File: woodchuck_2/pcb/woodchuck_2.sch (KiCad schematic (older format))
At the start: 31 parts

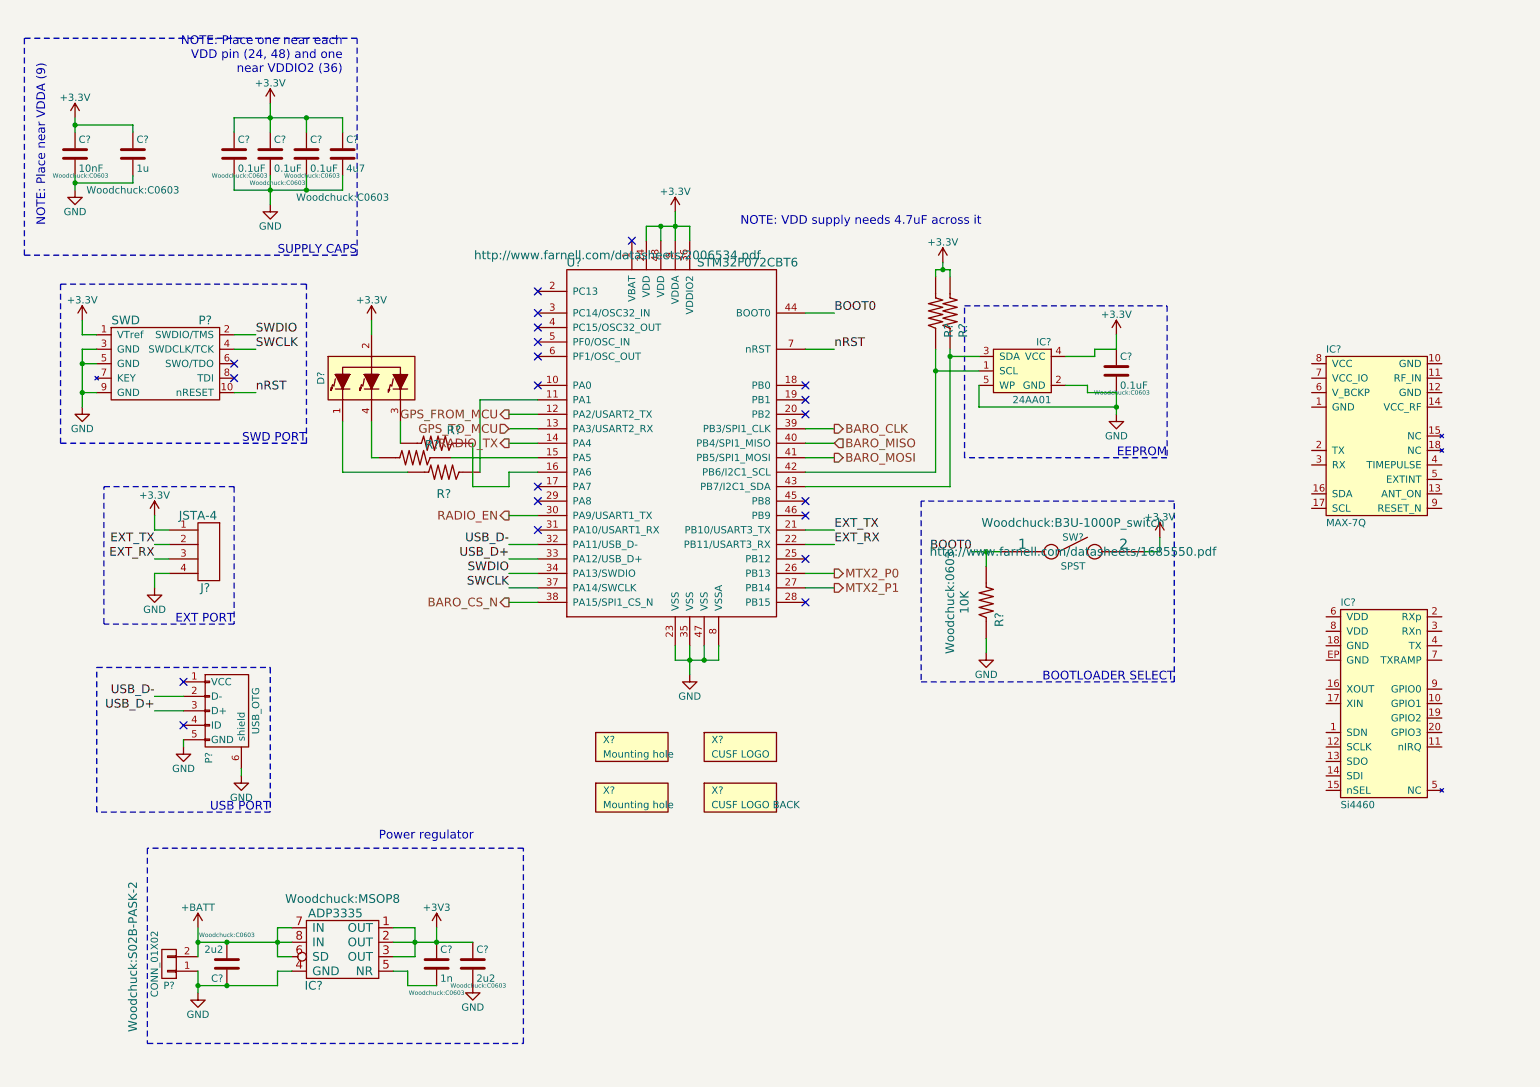
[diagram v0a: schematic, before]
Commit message: Tidy up files in branch, add radio and GPS to schematic, remove barometer, USART, USB
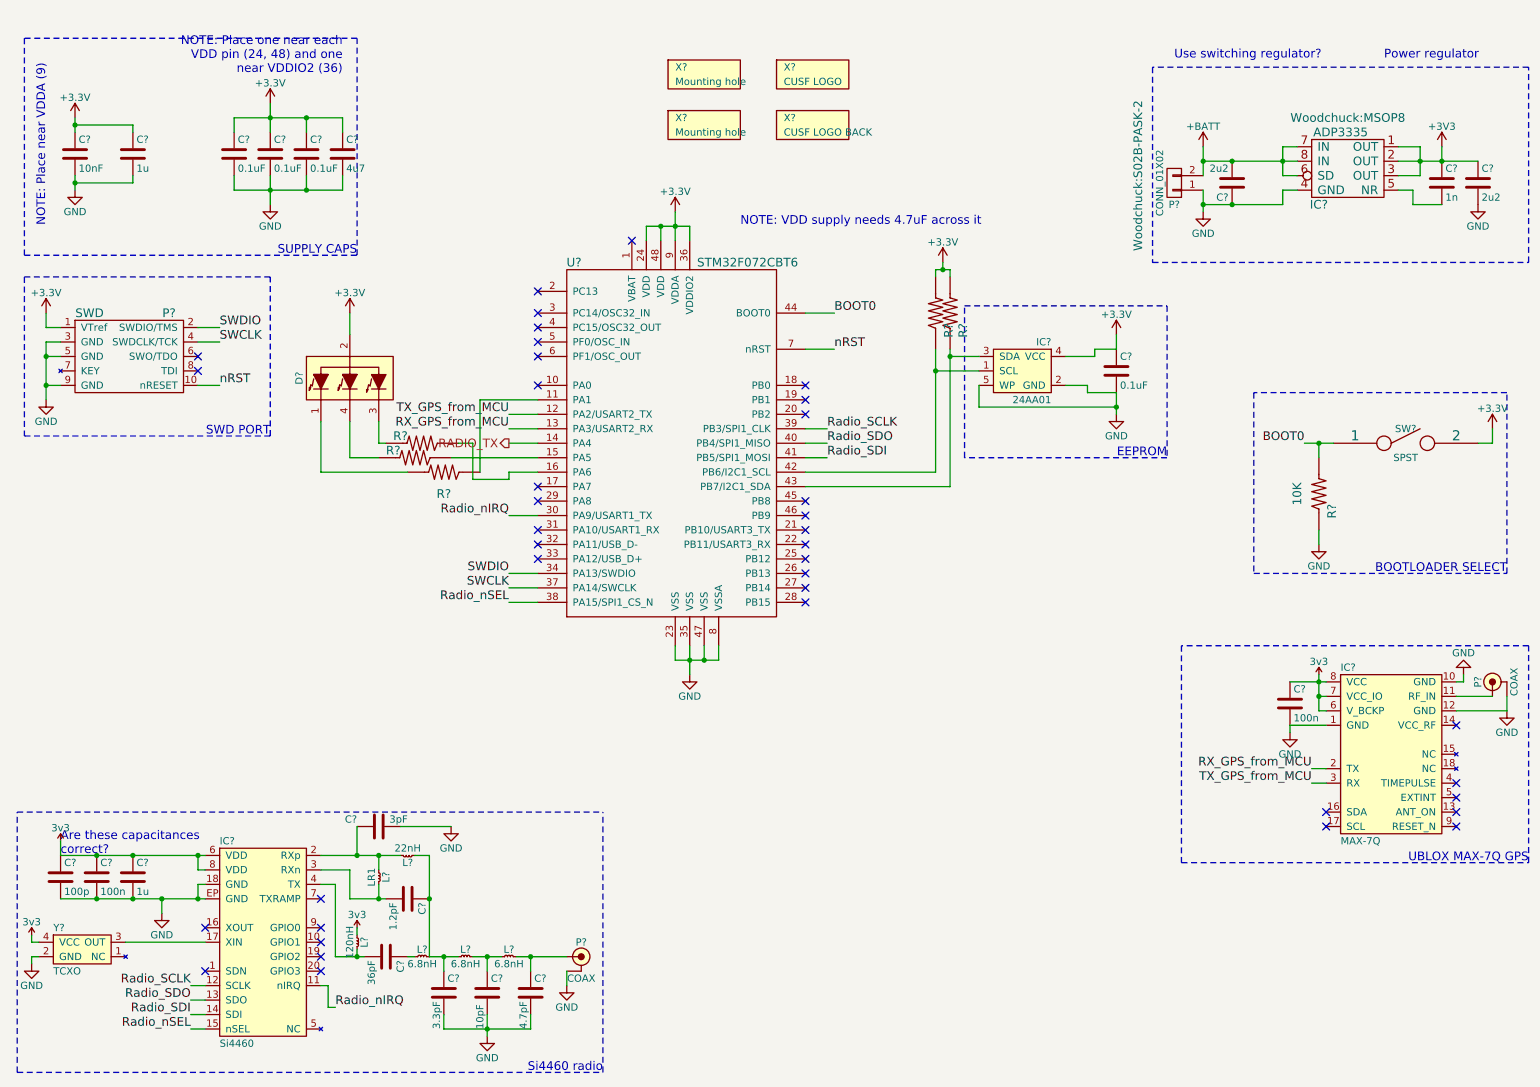
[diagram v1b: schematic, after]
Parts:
- removed J?: JSTA-4, Woodchuck:S04B-PASK-2, symbol JSTA-4
- removed P?: USB_OTG, Woodchuck:MOLEX_67503_1020_MINI_USB, symbol USB_OTG
- added C? (x2): 100n, agg:0402, symbol C
- added C?: 1u, agg:0402, symbol C
- added C?: 100p, agg:0402, symbol C
- added C?: 3pF, agg:0402, symbol C
- added C?: 1.2pF, agg:0402, symbol C
- added C?: 36pF, agg:0402, symbol C
- added C?: 3.3pF, agg:0402, symbol C
- added C?: 10pF, agg:0402, symbol C
- added C?: 4.7pF, agg:0402, symbol C
- added L?: LR1, agg:0603-L, symbol L
- added L?: 22nH, agg:0603-L, symbol L
- added L?: 120nH, agg:0603-L, symbol L
- added L? (x3): 6.8nH, agg:0603-L, symbol L
- added P? (x2): COAX, agg-unchecked:SMA-142-0701-801, symbol COAX
- added Y?: TCXO, symbol TCXO
- C? (x2): Digikey (none) -> Value; Farnell (none) -> Value; Fieldname (none) -> Value
- SW?: Digikey (none) -> Value; Fieldname (none) -> Value
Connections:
- net BARO_CLK is gone; now on net Radio_SCLK: U?.39 (PB3/SPI1_CLK)
- net BARO_CS_N is gone; now on net Radio_nSEL: U?.38 (PA15/SPI1_CS_N)
- net BARO_MISO is gone; now on net Radio_SDO: U?.40 (PB4/SPI1_MISO)
- net BARO_MOSI is gone; now on net Radio_SDI: U?.41 (PB5/SPI1_MOSI)
- net GPS_FROM_MCU is gone; now on net TX_GPS_from_MCU: U?.12 (PA2/USART2_TX)
- net GPS_TO_MCU is gone; now on net RX_GPS_from_MCU: U?.13 (PA3/USART2_RX)
- net RADIO_EN is gone; now on net Radio_nIRQ: U?.30 (PA9/USART1_TX)
- net GND: now also IC?.1 (GND), IC?.10 (GND), IC?.12 (GND), IC?.18 (GND), IC?.EP (GND), C?.2, C?.2, C?.2, C?.2, C?.2, C?.2, C?.2, C?.2, P?.2 (GND), P?.2 (GND), Y?.2 (GND)
- net at IC?.11 (RF_IN): now also P?.1 (RF)
- net RX_GPS_from_MCU: now reaches IC?.2 (TX)
- net TX_GPS_from_MCU: now reaches IC?.3 (RX)
- net 3v3: now reaches IC?.6 (V_BCKP)
- net 3v3: now also IC?.6 (VDD), IC?.7 (VCC_IO), IC?.8 (VCC), IC?.8 (VDD), C?.1, C?.1, C?.1, C?.1, L?.1, Y?.4 (VCC)
- net Radio_nIRQ: now reaches IC?.11 (nIRQ)
- net Radio_SCLK: now reaches IC?.12 (SCLK)
- net Radio_SDO: now reaches IC?.13 (SDO)
- net Radio_SDI: now reaches IC?.14 (SDI)
- net Radio_nSEL: now reaches IC?.15 (nSEL)
- net at IC?.17 (XIN): now also Y?.3 (OUT)
- net at IC?.2 (RXp): now also C?.1, L?.1, L?.2
- net at IC?.3 (RXn): now also C?.2, L?.2
- net at IC?.4 (TX): now also C?.2, L?.2
- net EXT_RX: no longer names the net of U?.22 (PB11/USART3_RX)
- net EXT_TX: no longer names the net of U?.21 (PB10/USART3_TX)
- net MTX2_P0: no longer names the net of U?.26 (PB13)
- net MTX2_P1: no longer names the net of U?.27 (PB14)
- net USB_D+: no longer names the net of U?.33 (PA12/USB_D+)
- net USB_D-: no longer names the net of U?.32 (PA11/USB_D-)
- new net: C?.1, C?.1, L?.1, L?.1, L?.2
- new net: C?.1, L?.1
- new net: C?.1, L?.1, L?.2
- new net: C?.1, L?.2, P?.1 (RF)
- no-connect marks 21 -> 39
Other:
- note added: "Are these capacitances\ncorrect?\n"
- note added: "Si4460 radio"
- note added: "UBLOX MAX-7Q GPS"
- note added: "Use switching regulator?"
- note removed: "EXT PORT"
- note removed: "USB PORT"
- moved on the sheet: C?, D?, IC?, P?, R?, SW?, X?

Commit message: Tidy up folders
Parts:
- removed D?: LED_RABG, Woodchuck:CREE_RGB_LED, symbol LED_RABG
- removed R?: 10K, Woodchuck:0603, symbol RESISTOR
- removed R? (x2): 510, Woodchuck:0603, symbol RESISTOR
- removed SW?: SPST, Woodchuck:B3U-1000P_switch, symbol SPST
- added D1: LED, symbol LED
- added R4: 10K, Woodchuck:0603, symbol RESISTOR
- added TP1: TESTPAD, agg:TESTPAD, symbol TESTPAD
- C4: renamed from C?; footprint Woodchuck:C0603 -> agg:0402; Farnell Value -> 2496814
- gave numbers to parts that had none: 42
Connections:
- net 3v3 is gone; now on net +3V3: C1.1, C18.1, C3.1, C5.1, IC1.6 (VDD), IC1.8 (VDD), IC4.6 (V_BCKP), IC4.7 (VCC_IO), IC4.8 (VCC), L1.1, Y1.4 (VCC)
- net +3V3: now also D1.2 (A)
- net GND: now also R4.1
- net Radio_nIRQ: now also U1.33 (PA12/USB_D+); no longer U1.30 (PA9/USART1_TX)
- net at R1.1: now also D1.1 (K)
- net BOOT0: no longer names the net of U1.44 (BOOT0)
- net BOOT0: now also R4.2, TP1.1 (TP)
- net RADIO_TX: no longer names the net of U1.14 (PA4)
- no-connect marks 39 -> 42
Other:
- note removed: "BOOTLOADER SELECT"
- note removed: "Use switching regulator?"
- moved on the sheet: R1

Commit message: Use KIPRJMOD in footprint library paths
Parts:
- IC4: footprint agg-unchecked:MAX-7Q -> unchecked:MAX-7Q; Digikey (none) -> Value; Farnell (none) -> Value; Fieldname (none) -> Value
- P2, P4: footprint agg-unchecked:SMA-142-0701-801 -> unchecked:SMA-142-0701-801; Digikey (none) -> Value; Fieldname (none) -> Value
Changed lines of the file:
@@
 F 0 "IC4" H 9700 5950 50  0000 L CNN
 F 1 "MAX-7Q" H 9700 4750 50  0000 L CNN
-F 2 "agg-unchecked:MAX-7Q" H 9700 4650 50  0001 L CNN
+F 2 "unchecked:MAX-7Q" H 9700 4650 50  0001 L CNN
 F 3 "" H 10050 5450 50  0001 C CNN
-F 4 "MAX-7Q" H 9700 4550 50  0001 L CNN "HabSupplies"
+F 4 "Value" H 10100 5450 60  0001 C CNN "Digikey"
+F 5 "Value" H 10100 5450 60  0001 C CNN "Farnell"
+F 6 "Value" H 10100 5450 60  0001 C CNN "Fieldname"
+F 7 "MAX-7Q" H 9700 4550 50  0001 L CNN "HabSupplies"
 	1    10100 5450
 	1    0    0    -1
@@
 F 0 "P4" H 10750 5150 50  0000 C CNN
 F 1 "COAX" H 10750 4900 50  0000 C CNN
-F 2 "agg-unchecked:SMA-142-0701-801" H 10750 4840 50  0001 C CNN
+F 2 "unchecked:SMA-142-0701-801" H 10750 4840 50  0001 C CNN
 F 3 "" H 10850 4950 50  0001 C CNN
-F 4 "1608592" H 10750 4770 50  0001 C CNN "Farnell"
+F 4 "Value" H 10750 5050 60  0001 C CNN "Digikey"
+F 5 "1608592" H 10750 4770 50  0001 C CNN "Farnell"
+F 6 "Value" H 10750 5050 60  0001 C CNN "Fieldname"
 	1    10750 5050
 	0    -1   -1   0
@@
 F 0 "P2" H 4450 7050 50  0000 C CNN
 F 1 "COAX" H 4450 6800 50  0000 C CNN
-F 2 "agg-unchecked:SMA-142-0701-801" H 4450 6740 50  0001 C CNN
+F 2 "unchecked:SMA-142-0701-801" H 4450 6740 50  0001 C CNN
 F 3 "" H 4550 6850 50  0001 C CNN
-F 4 "1608592" H 4450 6670 50  0001 C CNN "Farnell"
+F 4 "Value" H 4450 6950 60  0001 C CNN "Digikey"
+F 5 "1608592" H 4450 6670 50  0001 C CNN "Farnell"
+F 6 "Value" H 4450 6950 60  0001 C CNN "Fieldname"
 	1    4450 6950
 	1    0    0    -1

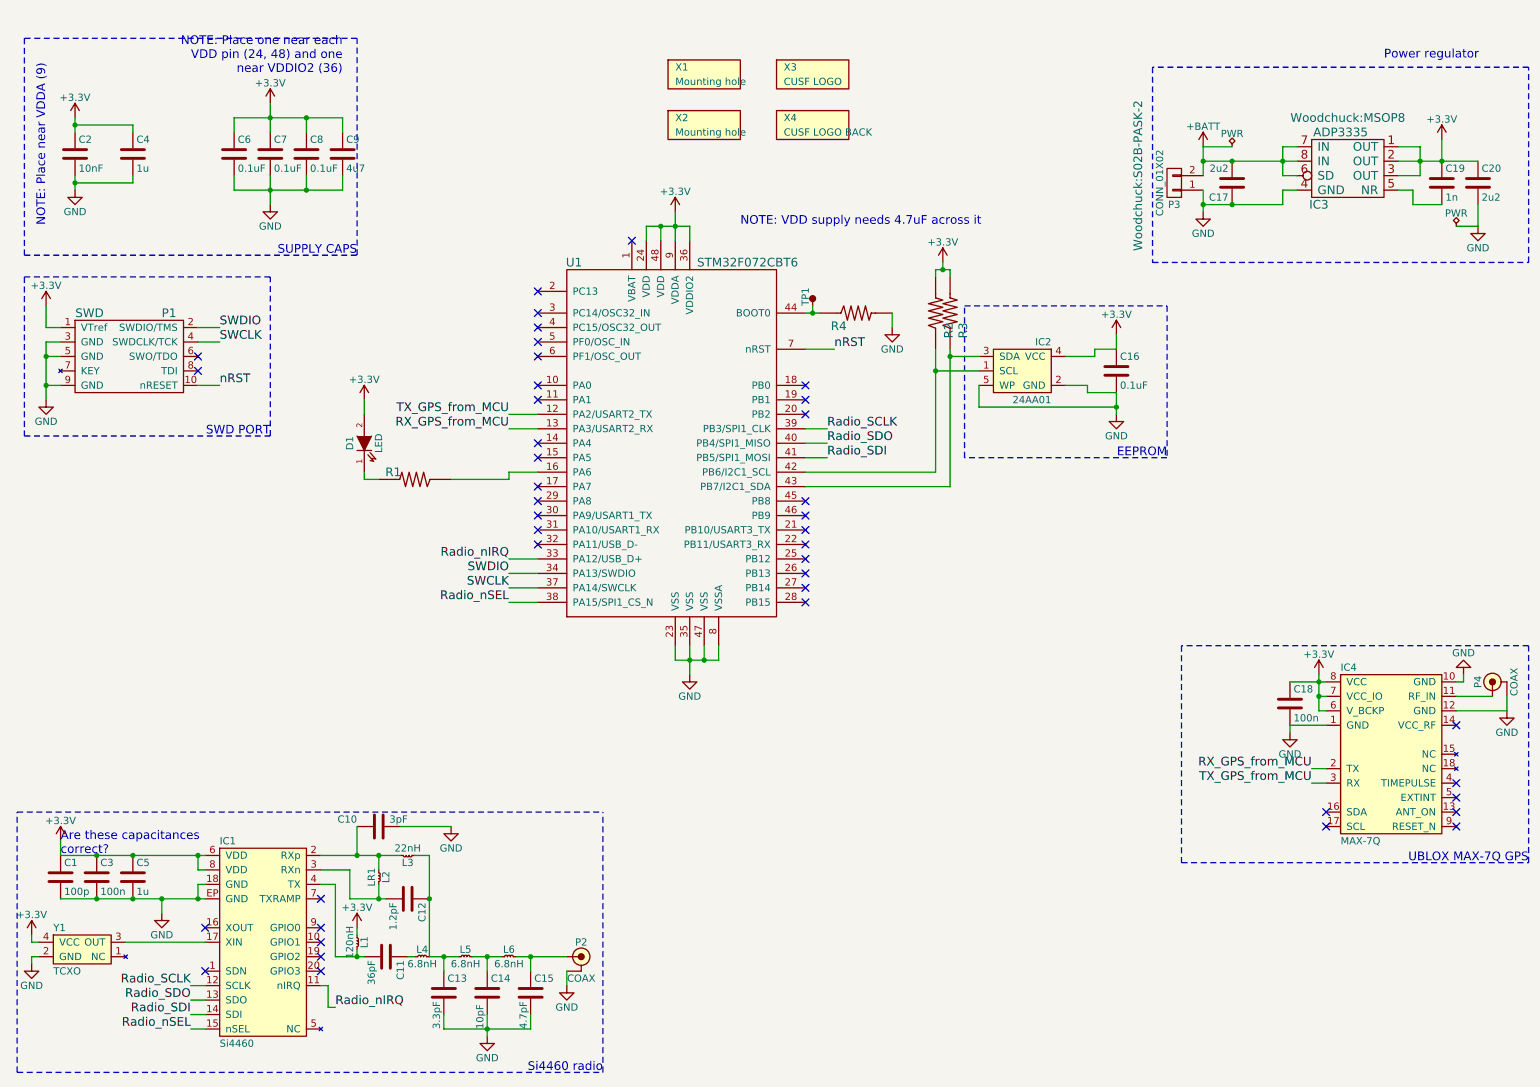
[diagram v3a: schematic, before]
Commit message: Change components to 0402, add farnell numbers and use different TCXO
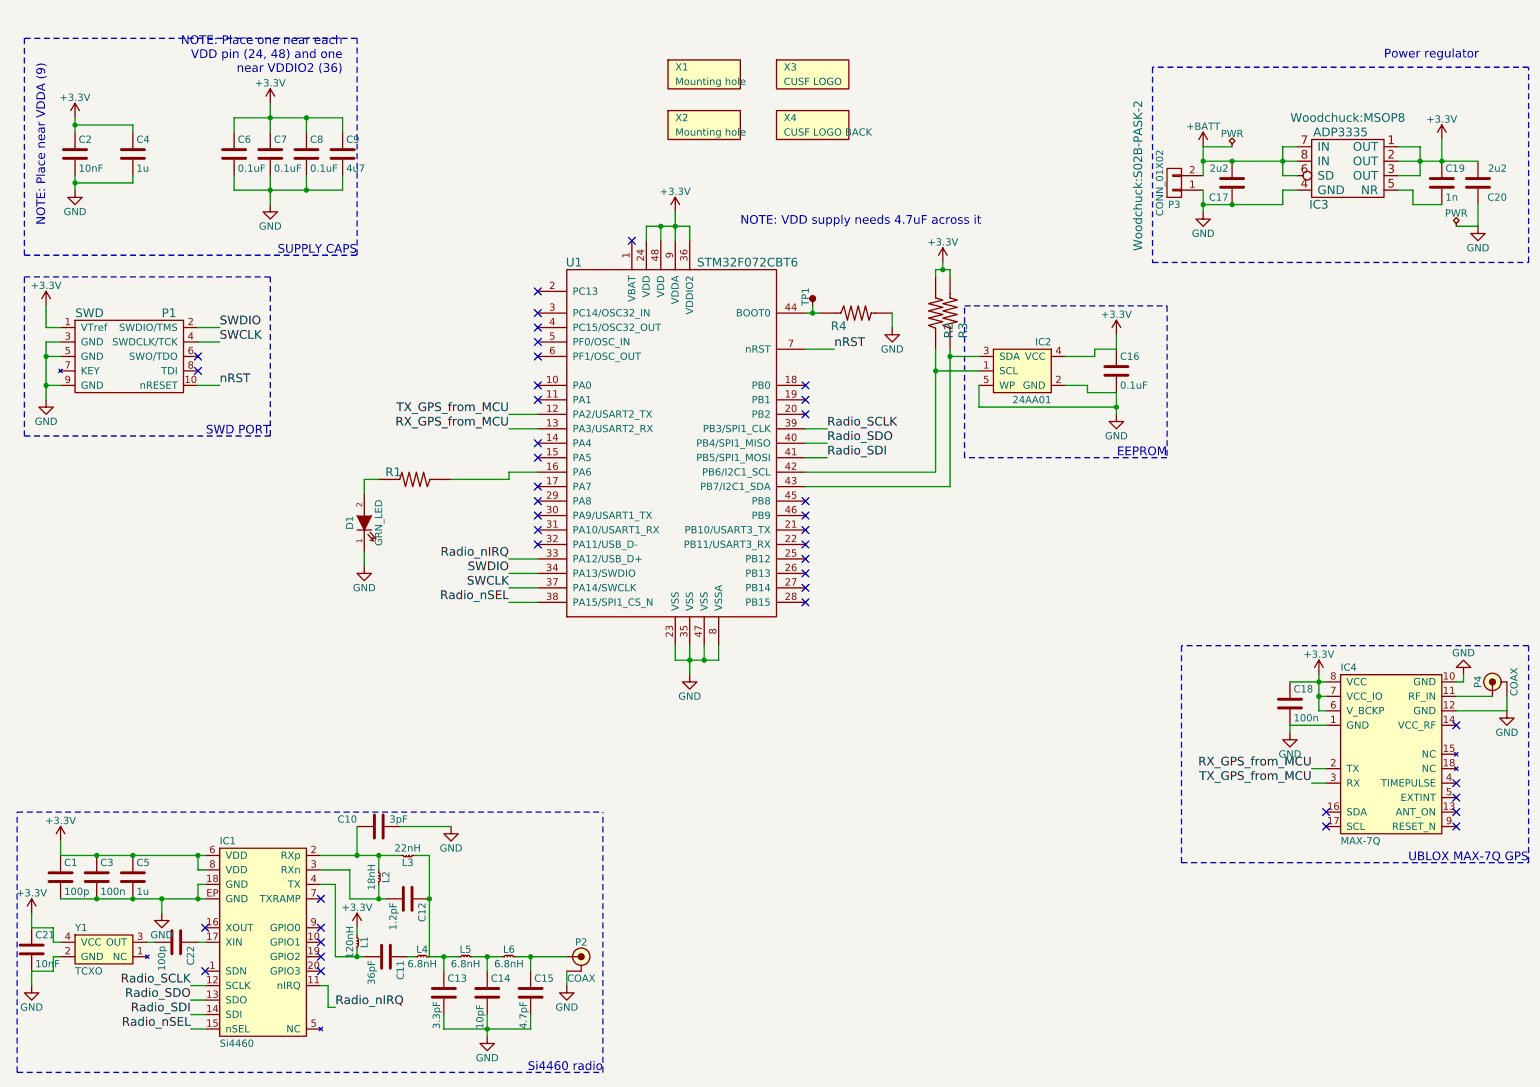
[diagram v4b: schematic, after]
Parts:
- added C21: 10nF, agg:0402, symbol C
- added C22: 100p, agg:0402, symbol C
- C1: Farnell Value -> 2496792
- C10: Farnell Value -> 2210752
- C11: Farnell Value -> 1865427
- C12: Farnell Value -> 2218843
- C13: Farnell Value -> 2434610
- C14: Farnell Value -> 2496790
- C15: Farnell Value -> 2434644
- C16, C6, C7, C8: footprint Woodchuck:C0603 -> agg:0402; Farnell 1759037 -> 2496771
- C17, C20: footprint Woodchuck:C0603 -> agg:0603; Farnell 2211185 -> 2332678
- C18, C3: Farnell Value -> 2496771
- C19: footprint Woodchuck:C0603 -> agg:0402; Farnell 1759088 -> 2280640
- C2: footprint Woodchuck:C0603 -> agg:0402; Farnell 1907314 -> 1414575
- C5: Farnell Value -> 2496814
- C9: footprint Woodchuck:C0603 -> agg:0402; Farnell Value -> 2426952
- D1: value LED -> GRN_LED; footprint (none) -> agg:0603-LED; Digikey (none) -> Value; Farnell (none) -> 2290328; Fieldname (none) -> Value
- L2: value LR1 -> 18nH; Farnell Value -> 2424720
- R1: footprint Woodchuck:0603 -> agg:0402; Farnell 1469826 -> 2073095
- R2, R3, R4: footprint Woodchuck:0603 -> agg:0402; Farnell 9331700 -> 2072517
- Y1: footprint (none) -> Woodchuck:TG-5006CJ; Farnell 2405785 -> 2428493
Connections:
- net +3V3: now also C20.2, C21.1; no longer C20.1, D1.2 (A)
- net GND: now also C20.1, D1.1 (K), C21.2; no longer C20.2
- net at IC1.17 (XIN): now also C22.1; no longer Y1.3 (OUT)
- net at R1.1: now also D1.2 (A); no longer D1.1 (K)
- new net: C22.2, Y1.3 (OUT)
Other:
- note removed: "Are these capacitances\ncorrect?\n"
- moved on the sheet: D1, Y1
